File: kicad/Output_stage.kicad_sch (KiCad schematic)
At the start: 43 parts

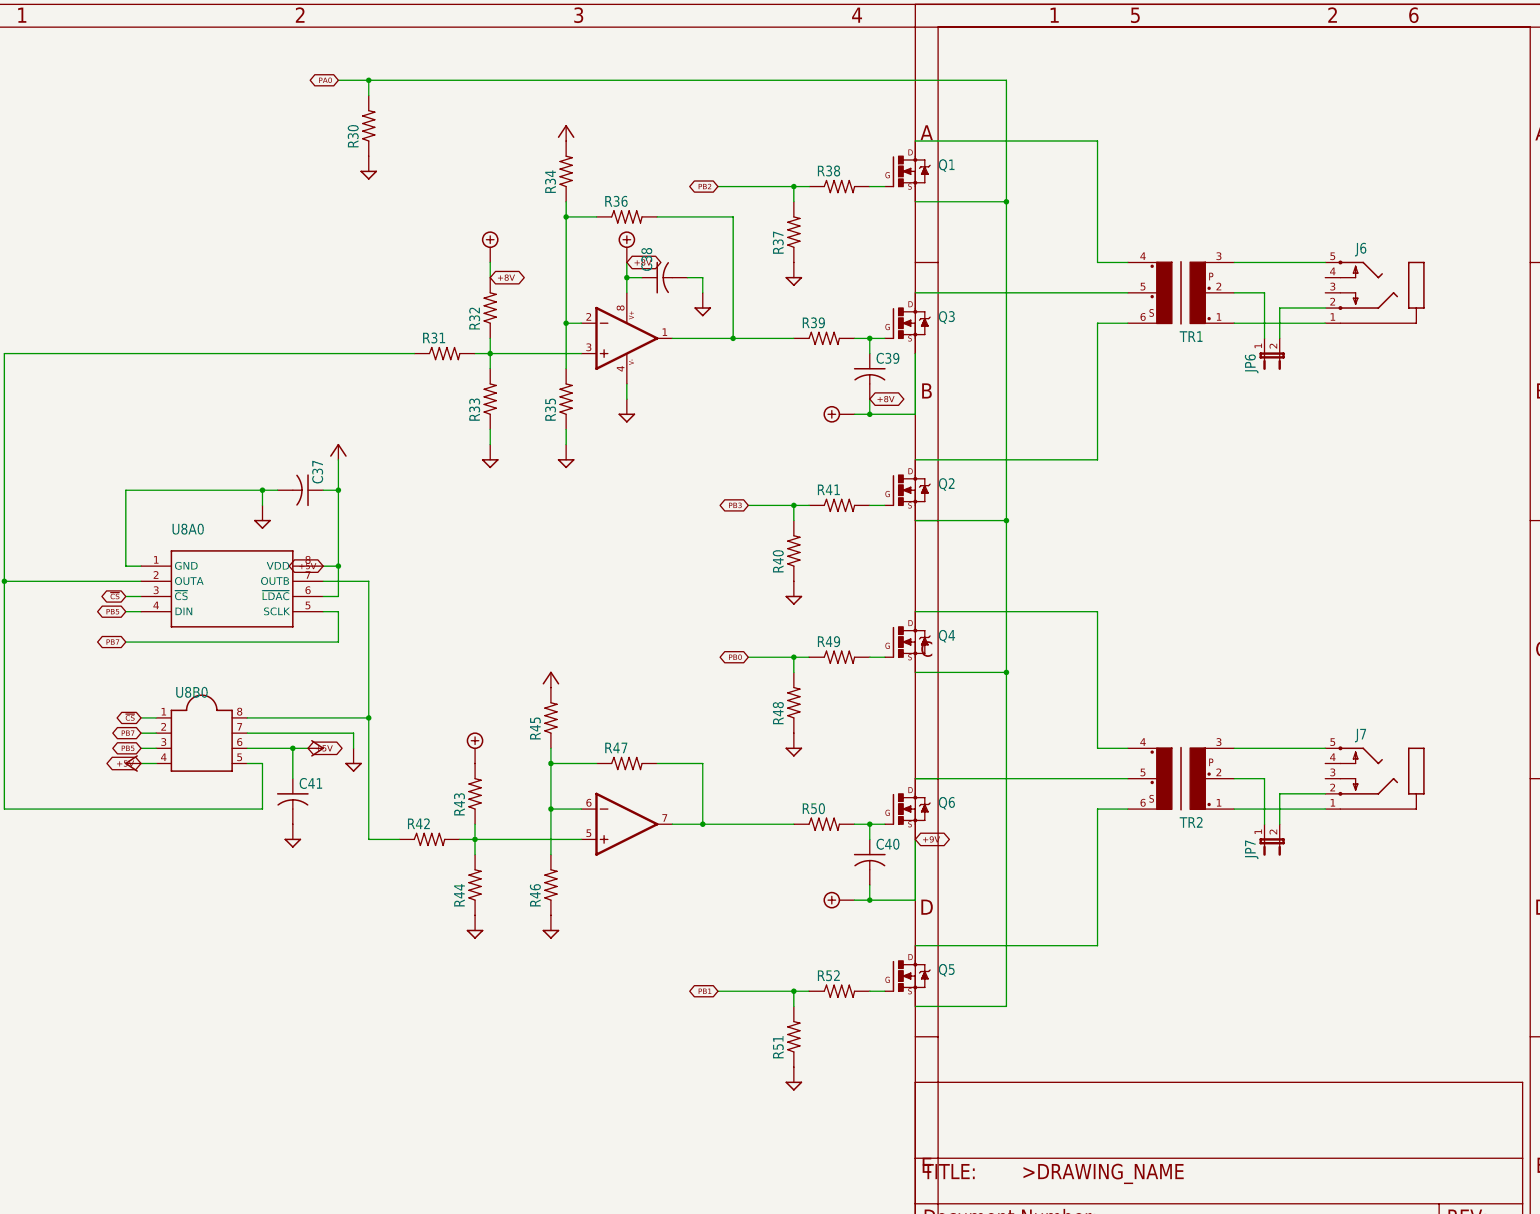
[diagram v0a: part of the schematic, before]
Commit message: Conversion of display print to KiCad components; still attached to main board
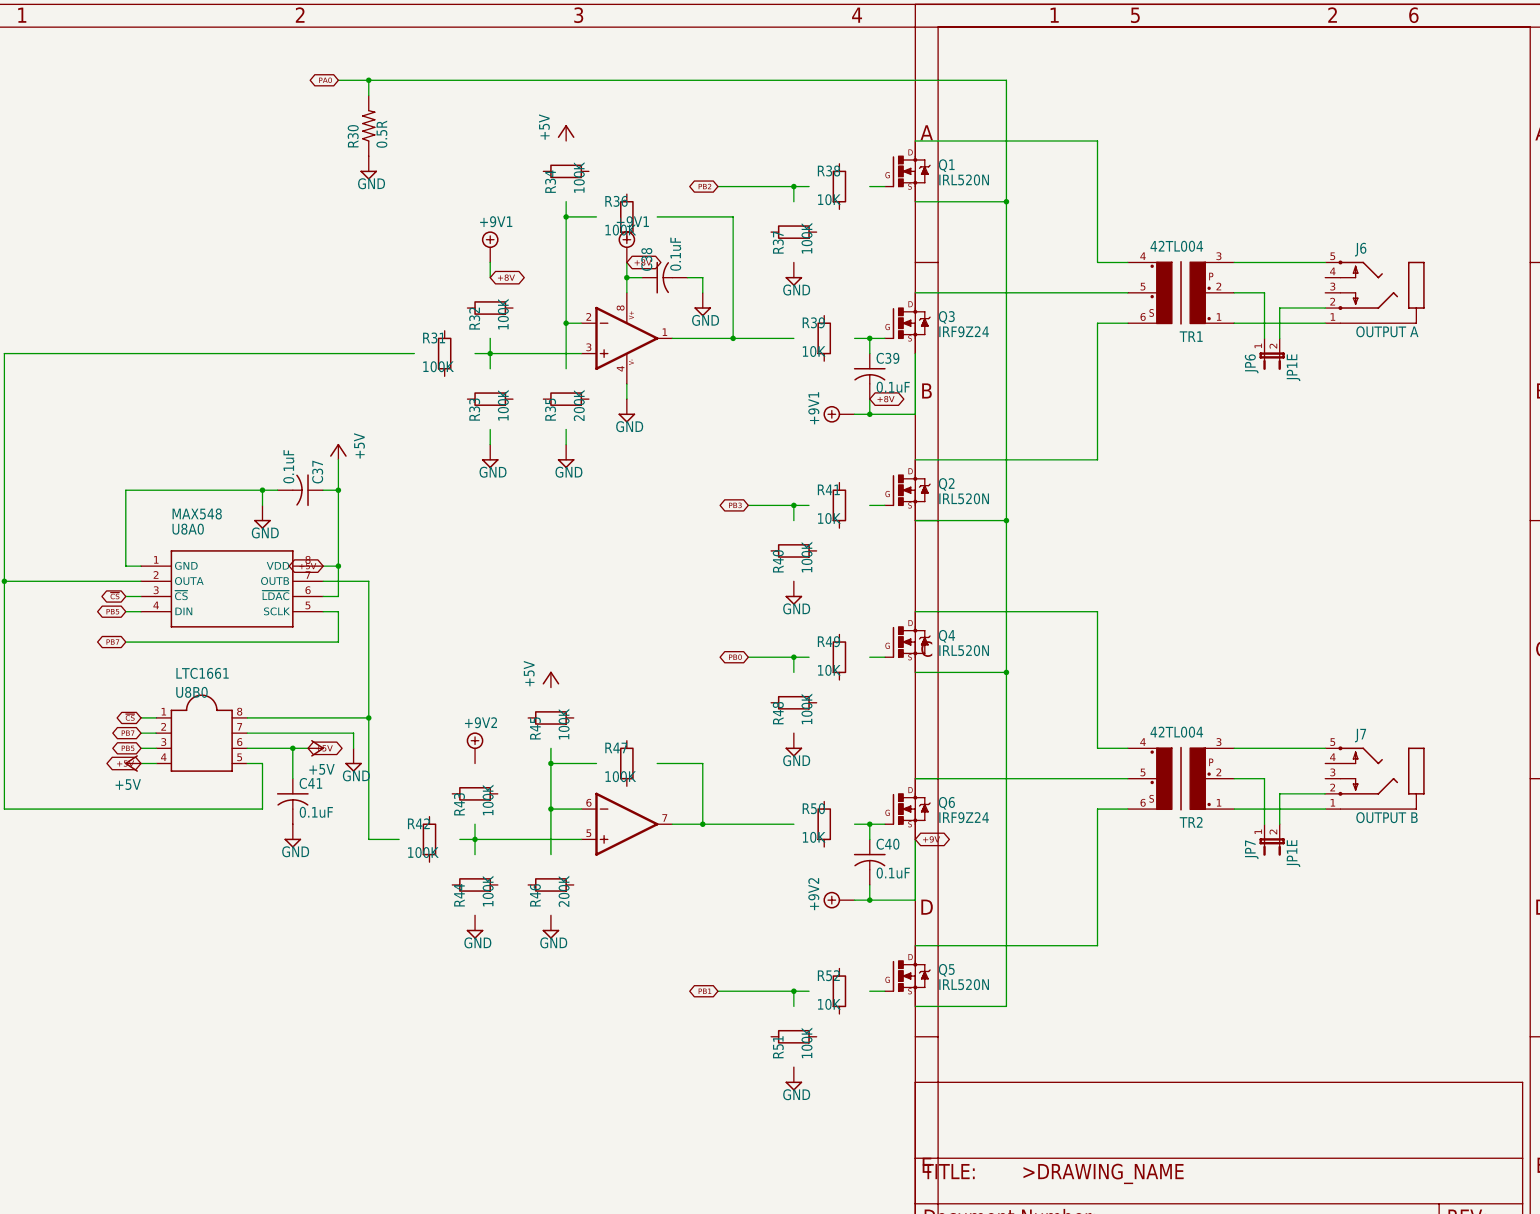
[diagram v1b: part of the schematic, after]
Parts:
- C37, C38, C39, C40, C41: value (none) -> 0.1uF; footprint (none) -> mk312:C025-024X044
- J6: value (none) -> OUTPUT A; footprint (none) -> mk312:STX3100
- J7: value (none) -> OUTPUT B; footprint (none) -> mk312:STX3100
- JP6, JP7: value (none) -> JP1E; footprint (none) -> mk312:JP1
- Q1, Q2, Q4, Q5: value (none) -> IRL520N; footprint (none) -> mk312:TO220V
- Q3, Q6: value (none) -> IRF9Z24; footprint (none) -> mk312:TO220V
- R30: value (none) -> 0.5R; footprint (none) -> mk312:0309_12
- R31, R32, R33, R34, R36, R37, R40, R42, R43, R44, R45, R47, R48, R51: value (none) -> 100K; footprint (none) -> mk312:0207_10; symbol mk312-eagle-import:R-US_0207/10 -> Device:R
- R35, R46: value (none) -> 200K; footprint (none) -> mk312:0207_10; symbol mk312-eagle-import:R-US_0207/10 -> Device:R
- R38, R39, R41, R49, R50, R52: value (none) -> 10K; footprint (none) -> mk312:0207_10; symbol mk312-eagle-import:R-US_0207/10 -> Device:R
- TR1, TR2: value (none) -> 42TL004; footprint (none) -> mk312:42TL
- U10: value (none) -> LM358N; footprint (none) -> mk312:DIL08
- U8A0: value (none) -> MAX548; footprint (none) -> mk312:DIL08
- U8B0: value (none) -> LTC1661; footprint (none) -> mk312:SOCKET-08
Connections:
- net +8V: no longer R32.2
- net +9V: no longer R43.2
- net GND: no longer R33.1, R35.1, R37.1, R40.1, R44.1, R46.1, R48.1, R51.1
- net PB0: no longer R48.2, R49.1
- net PB1: no longer R51.2, R52.1
- net PB2: no longer R37.2, R38.1
- net PB3: no longer R40.2, R41.1
- net VCC: no longer R34.2, R45.2
- net at C40.1, Q6.1 (G): no longer R50.2
- net at R52.2: no longer Q5.1 (G)
- net at U8A0.2 (OUTA), U8B0.5: no longer R31.1
- net at C39.1, Q3.1 (G): no longer R39.2
- net at R41.2: no longer Q2.1 (G)
- net at U8A0.7 (OUTB), U8B0.8: no longer R42.1
- net at Q1.1 (G): no longer R38.2
- net at Q4.1 (G): no longer R49.2
- now unconnected: R31.2, R32.1, R33.2, R34.1, R35.2, R36.1, R36.2, R39.1, R42.2, R43.1, R44.2, R45.1, R46.2, R47.1, R47.2, R50.1, U10.1 (OUT), U10.2 (-IN), U10.3 (+IN), U10.5 (+IN), U10.6 (-IN), U10.7 (OUT)
